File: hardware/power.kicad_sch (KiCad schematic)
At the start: 41 parts, among them J15 Conn_01x02, Q13 AO3401A, Q14 BC817W, U7 ZTP7193MA, U8 ZTP7193MA

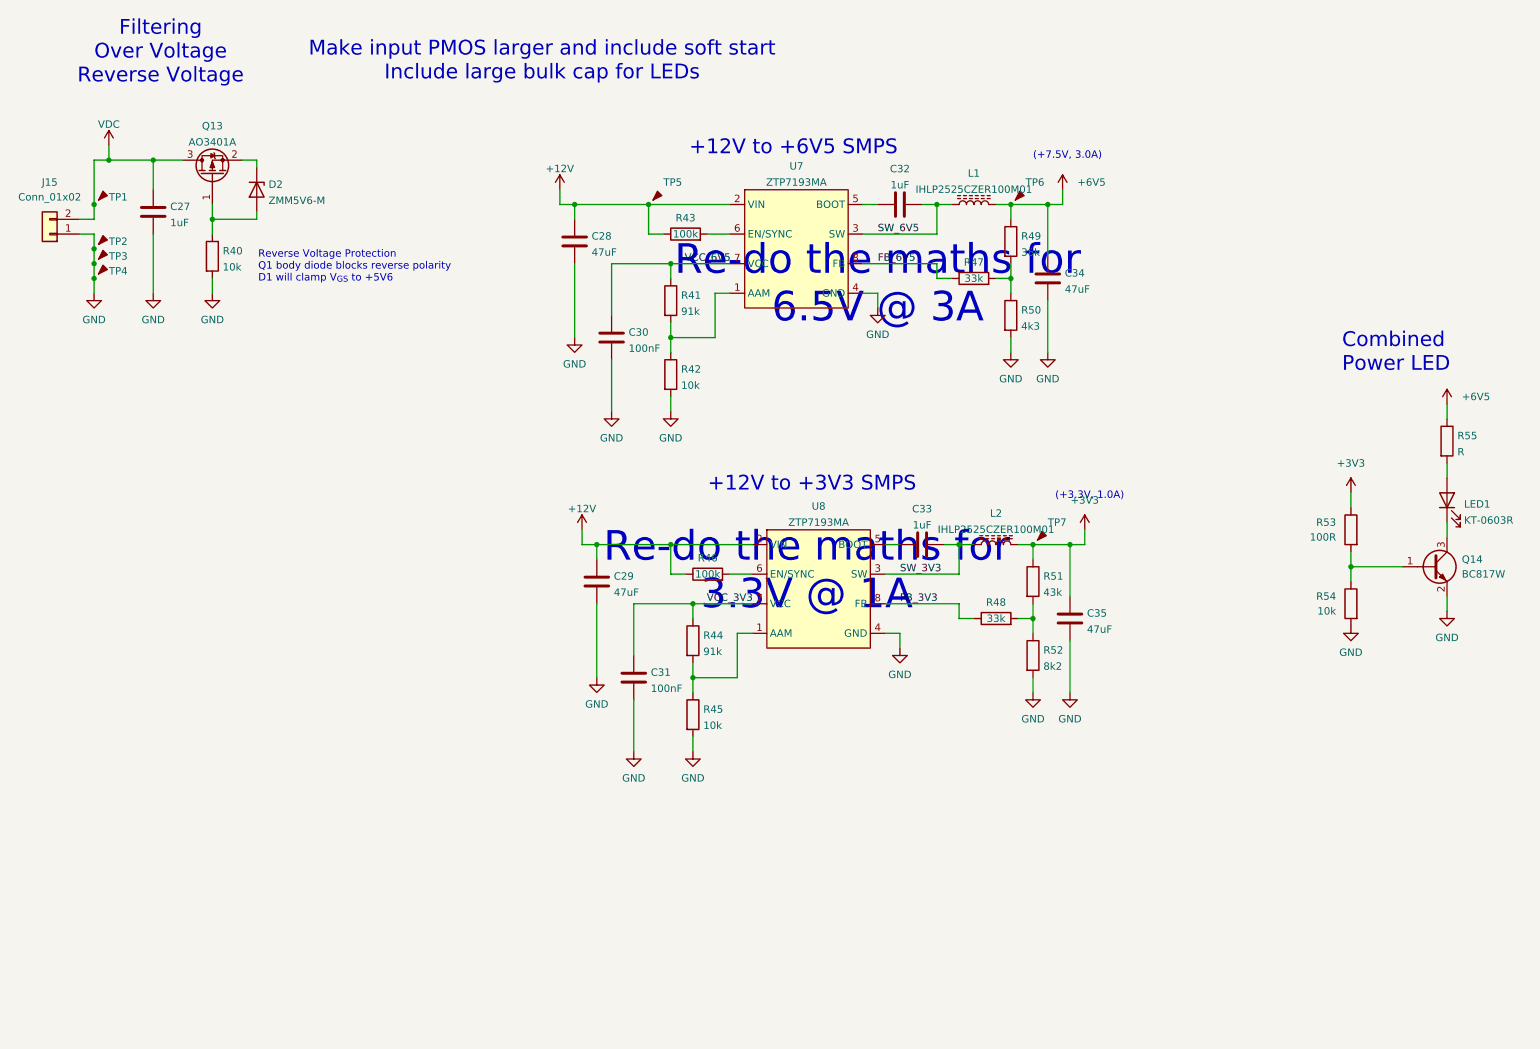
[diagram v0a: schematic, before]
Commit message: adding ESP32 and PSU options
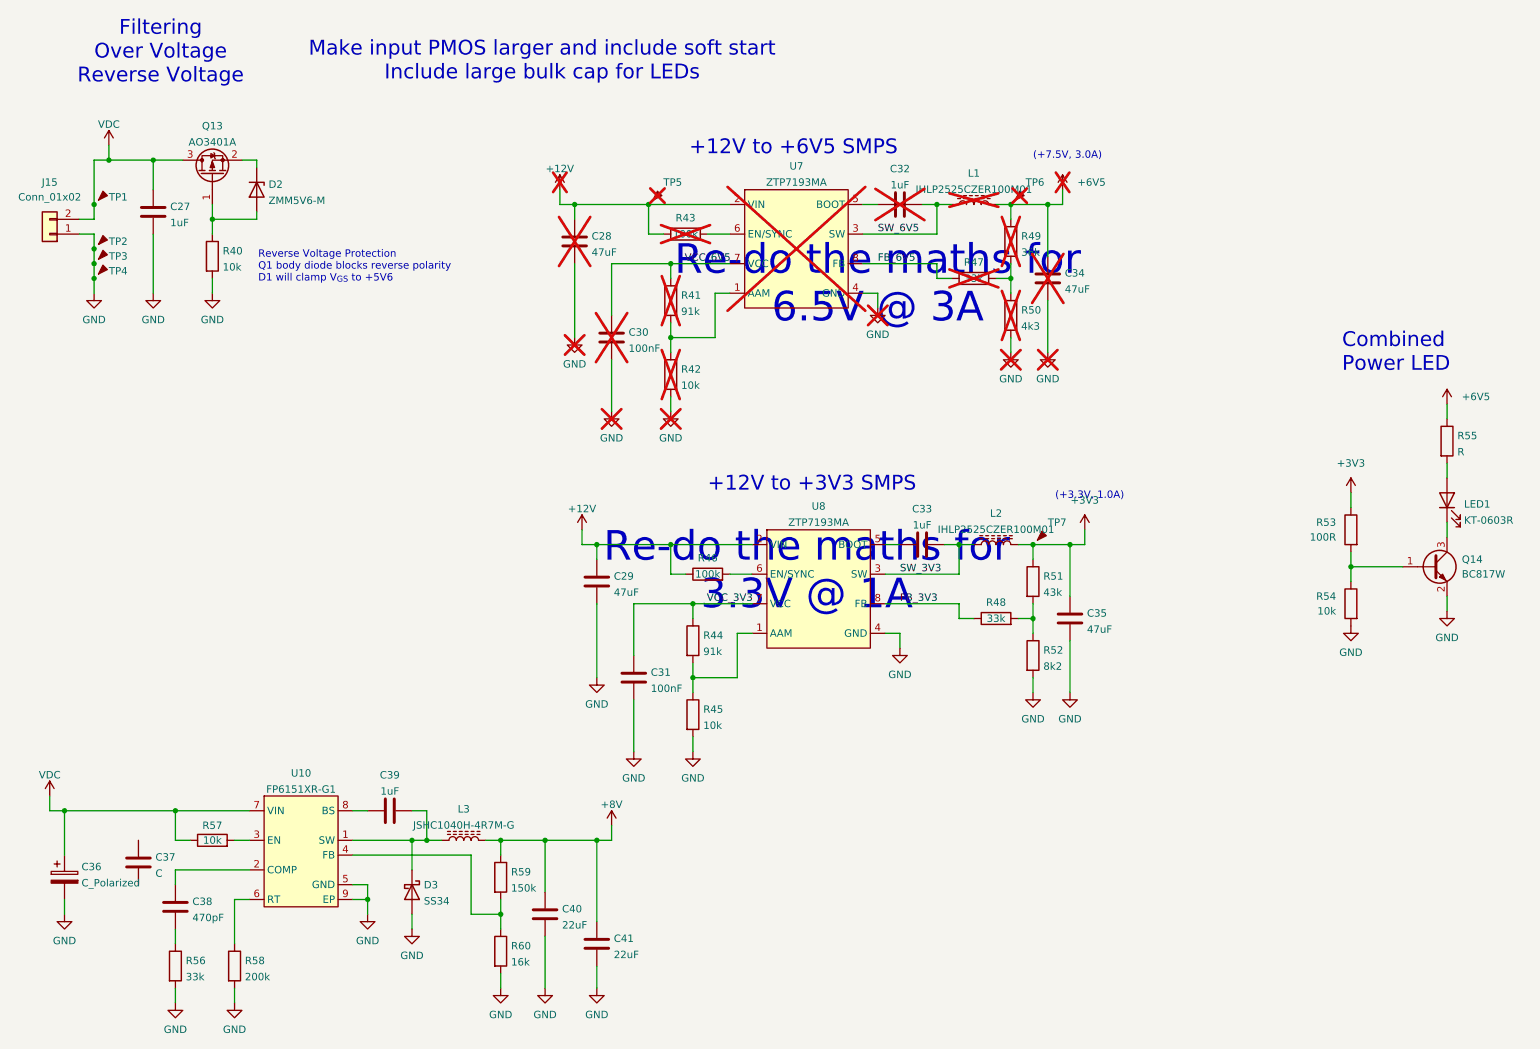
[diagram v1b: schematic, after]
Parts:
- added C36: C_Polarized, symbol Device:C_Polarized
- added C37: C, Capacitor_SMD:C_1210_3225Metric, symbol Device:C
- added C38: 470pF, Capacitor_SMD:C_0603_1608Metric, symbol Device:C
- added C39: 1uF, Capacitor_SMD:C_0603_1608Metric, symbol Device:C
- added C40, C41: 22uF, Capacitor_SMD:C_1206_3216Metric, symbol Device:C
- added D3: SS34, Diode_SMD:D_SMA, symbol Device:D_Schottky
- added L3: JSHC1040H-4R7M-G, Inductor_SMD:L_Wuerth_HCI-1040, symbol Device:L_Ferrite
- added R56: 33k, Resistor_SMD:R_0603_1608Metric, symbol Device:R
- added R57: 10k, Resistor_SMD:R_0603_1608Metric, symbol Device:R
- added R58: 200k, Resistor_SMD:R_0603_1608Metric, symbol Device:R
- added R59: 150k, Resistor_SMD:R_0603_1608Metric, symbol Device:R
- added R60: 16k, Resistor_SMD:R_0603_1608Metric, symbol Device:R
- added U10: FP6151XR-G1, Package_SO:HSOP-8-1EP_3.9x4.9mm_P1.27mm_EP2.41x3.1mm, symbol Pinski1_Parts:FP6151XR-G1
- C28, C30, C32, C34, L1, R41, R42, R43, R47, R49, R50, TP5, TP6, U7: now not fitted
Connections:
- net GND: now also C36.2, C40.2, C41.2, D3.2 (A), R56.2, R58.2, R60.2, U10.5 (GND), U10.9 (EP)
- net VDC: now also C36.1, R57.1, U10.7 (VIN)
- new net: R57.2, U10.3 (EN)
- new net: R58.1, U10.6 (RT)
- new net: C38.1, U10.2 (COMP)
- new net: C38.2, R56.1
- new net: C39.1, U10.8 (BS)
- new net: C39.2, D3.1 (K), L3.1, U10.1 (SW)
- new net: R59.2, R60.1, U10.4 (FB)
- new net +8V: C40.1, C41.1, L3.2, R59.1
